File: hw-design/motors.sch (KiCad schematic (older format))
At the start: 20 parts, among them P4 left_motor, P5 right_motor, Q1 BC847, U2 TCS3472, U5 drv8835, U6 drv8835, U9 TCS3472

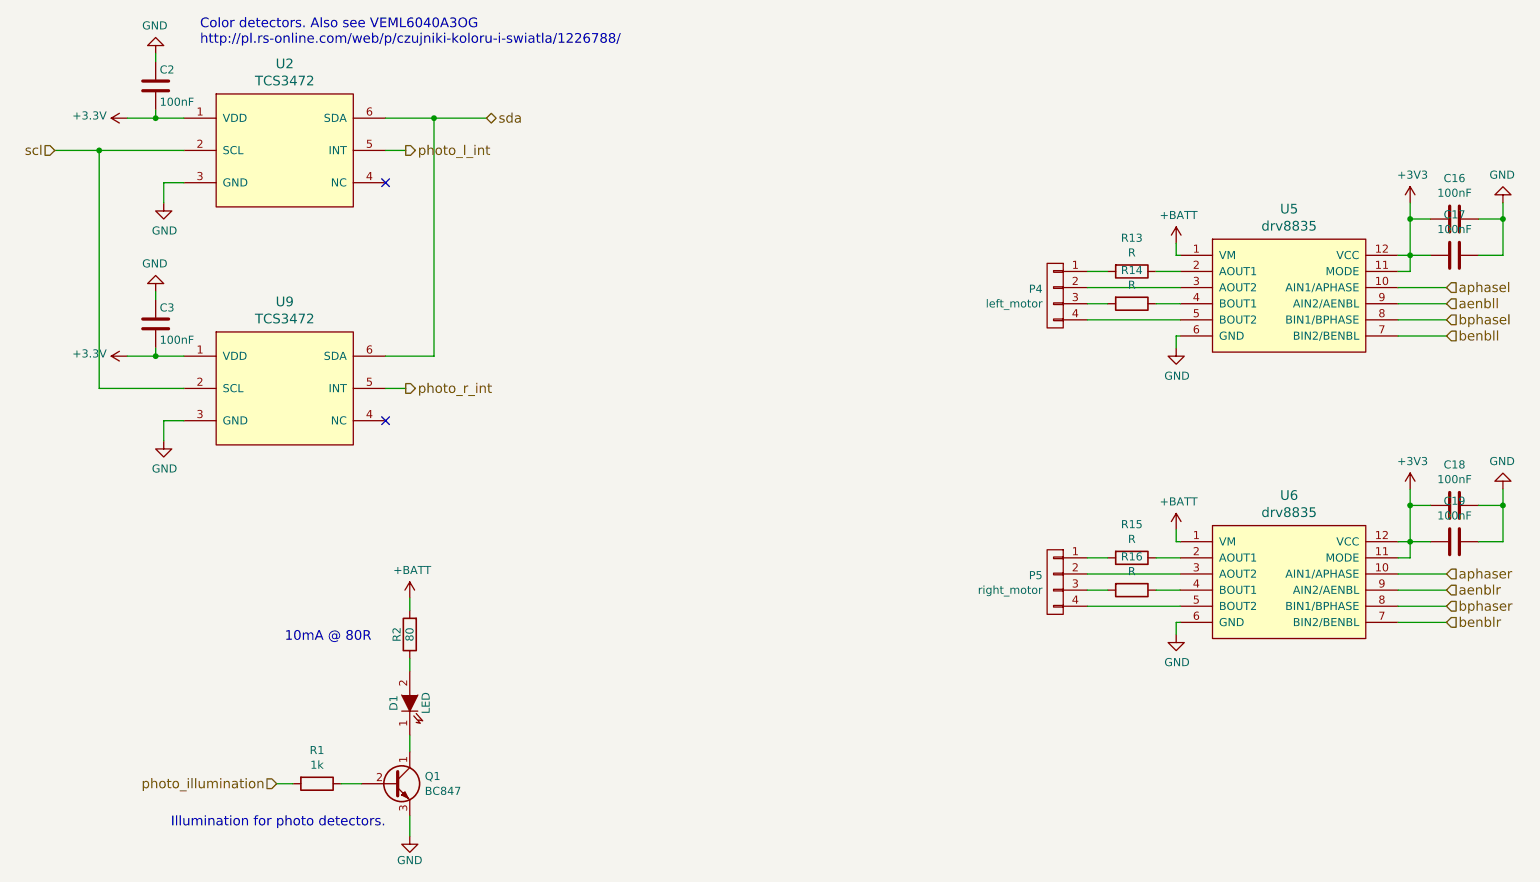
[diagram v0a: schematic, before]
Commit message: Another idea of PCB split.
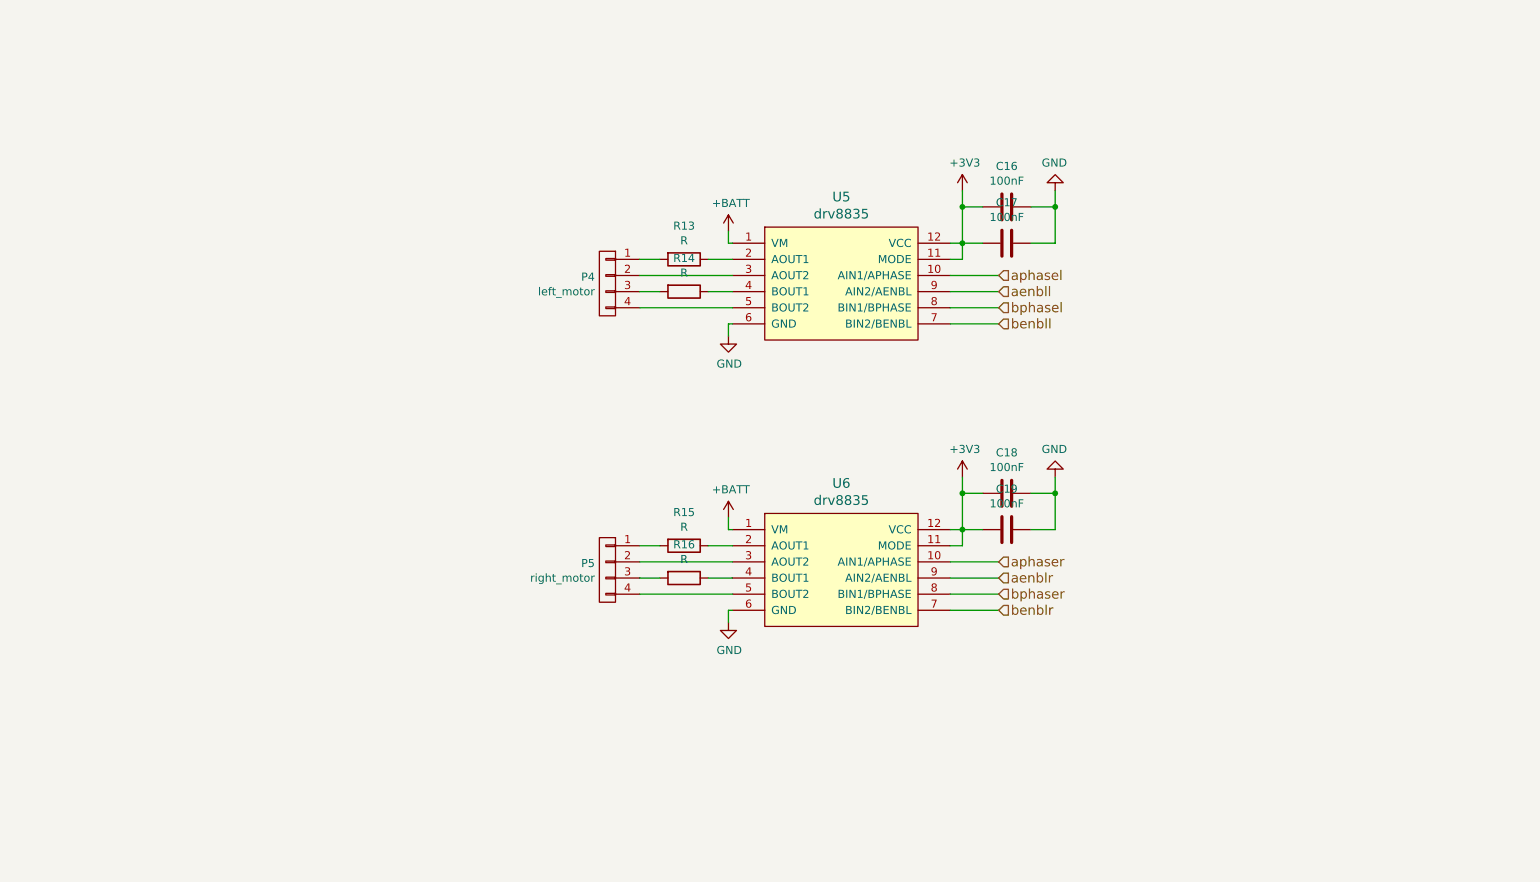
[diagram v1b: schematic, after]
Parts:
- removed C2, C3: 100nF, w_smd_cap:c_0603, symbol C
- removed D1: LED, LEDs:LED_0805, symbol LED
- removed Q1: BC847, w_smd_trans:sot23, symbol Q_NPN_CBE
- removed R1: 1k, w_smd_resistors:r_0402, symbol R
- removed R2: 80, w_smd_resistors:r_0603, symbol R
- removed U2, U9: TCS3472, iwasz:SC70-6, symbol TCS3472
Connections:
- no-connect marks 2 -> 0
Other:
- note removed: "10mA @ 80R"
- note removed: "Color detectors. Also see VEML6040A3OG\nhttp://pl.rs-online.com/web/p/czujniki-koloru-i-swiatla/1226788/"
- note removed: "Illumination for photo detectors."
- moved on the sheet: C16, C17, C18, C19, P4, P5, R13, R14, R15, R16, U5, U6
